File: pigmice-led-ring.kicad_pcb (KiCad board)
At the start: 2 copper layers, 46 x 51 mm, 46 parts, among them J1 Conn_01x02_Female, J2 Conn_01x03_Female, U1 LMR62014XMF

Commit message: Move labels a bit
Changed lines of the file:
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@@
     (tags SOT-23-5)
     (attr smd)
-    (fp_text reference U1 (at 1.972 -2.162839) (layer F.SilkS)
+    (fp_text reference U1 (at 2.099 -2.162839) (layer F.SilkS)
       (effects (font (size 0.75 0.75) (thickness 0.15)))
     )
@@
     (tags resistor)
     (attr smd)
-    (fp_text reference R2 (at 0 1.4 270) (layer F.SilkS)
-      (effects (font (size 0.75 0.75) (thickness 0.15)))
+    (fp_text reference R2 (at 0.044 1.585 270) (layer F.SilkS)
+      (effects (font (size 1 1) (thickness 0.15)))
     )
     (fp_text value 13.3k (at 0 1.65 90) (layer F.Fab)
@@
     (tags capacitor)
     (attr smd)
-    (fp_text reference CF1 (at 1.515 -1.934) (layer F.SilkS)
+    (fp_text reference CF1 (at 1.515 -1.807) (layer F.SilkS)
       (effects (font (size 0.75 0.75) (thickness 0.15)))
     )

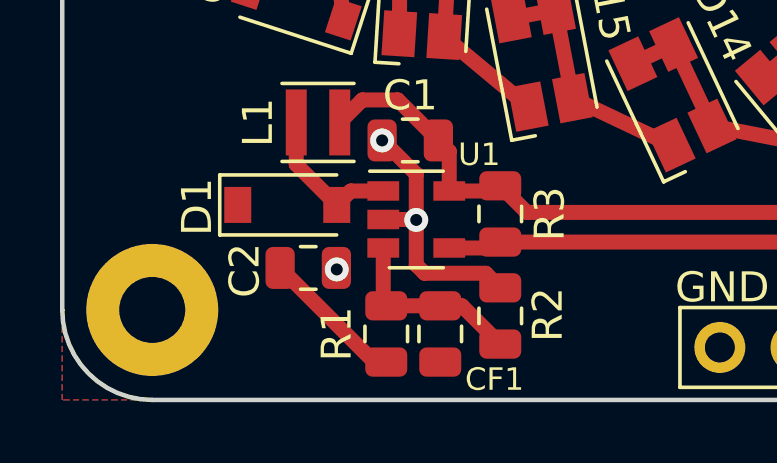
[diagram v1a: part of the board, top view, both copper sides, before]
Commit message: Remove extraneous trace
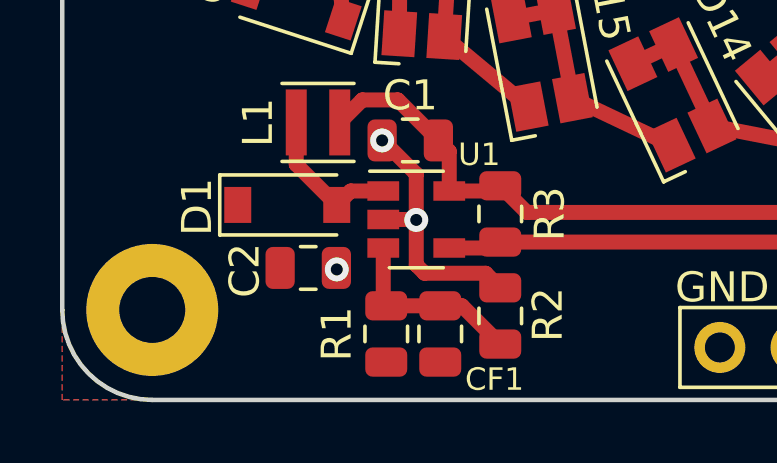
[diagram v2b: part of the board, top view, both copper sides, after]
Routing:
- net /Vled: track 4.84 -> 0.40 mm
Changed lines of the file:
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@@
     (thickness 1.6)
     (drawings 14)
-    (tracks 133)
+    (tracks 132)
     (zones 0)
     (modules 46)
@@
   (via (at 77.6625 99.35) (size 0.8) (drill 0.4) (layers F.Cu B.Cu) (net 1) (status 30))
   (segment (start 77.4 106.7375) (end 77.8 106.7375) (width 0.5) (layer F.Cu) (net 2) (status 30))
-  (segment (start 74.2625 103.6) (end 77.4 106.7375) (width 0.5) (layer F.Cu) (net 2) (status 30))
   (segment (start 77.7 104.7625) (end 77.8 104.8625) (width 0.5) (layer F.Cu) (net 3) (status 30))
   (segment (start 77.7 102.934839) (end 77.7 104.7625) (width 0.5) (layer F.Cu) (net 3) (status 30))

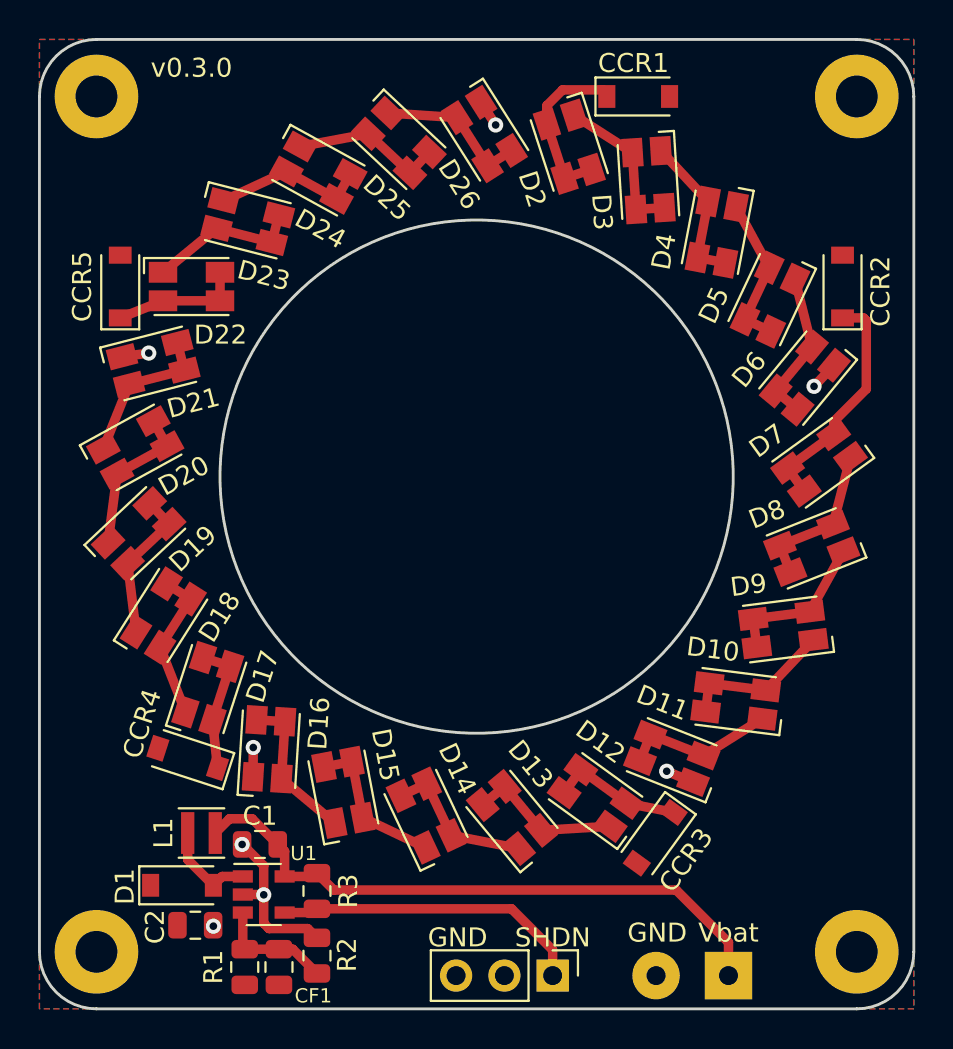
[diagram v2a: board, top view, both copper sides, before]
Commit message: Revision 0.3.1
- Fixes an issue in the LED footprint resulting in a short between the
anode and cathode
- Uses thicker traces where possible
- Moves CCRs for better connections to Vled plane
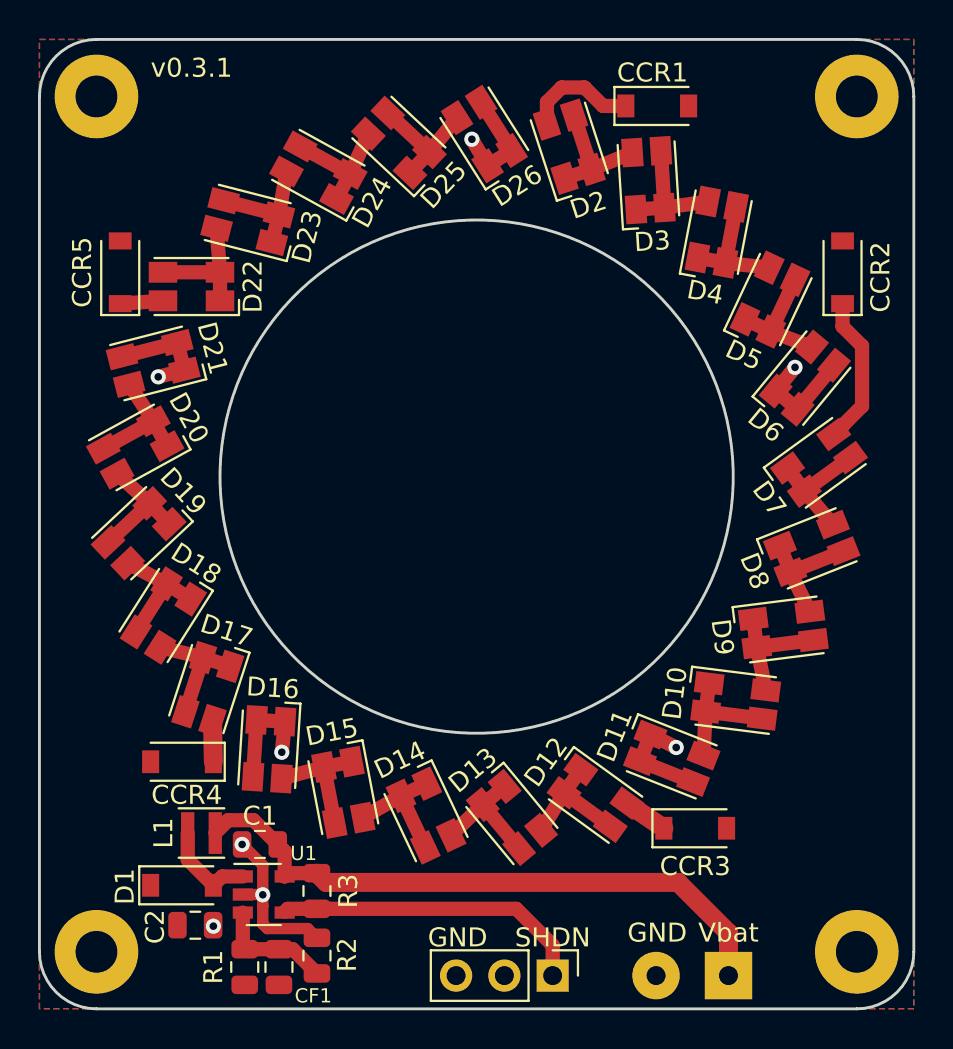
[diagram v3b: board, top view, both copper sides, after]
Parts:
- moved CCR3 2.16 mm to (101.5, 98.5), turned to 0 degrees
- moved CCR1 1.12 mm to (99.5, 60.5)
- moved CCR2 0.75 mm to (109.2, 69.2)
- moved CCR5 0.75 mm to (71.2, 69.2)
- moved CCR4 0.36 mm to (74.5, 95.0), turned to 180 degrees
- turned D10 to 352.8 degrees
- turned D11 to 338.4 degrees
- turned D12 to 324 degrees
- turned D13 to 309.6 degrees
- turned D14 to 295.2 degrees
- turned D15 to 280.8 degrees
- turned D16 to 266.4 degrees
- turned D17 to 252 degrees
- turned D18 to 237.6 degrees
- turned D19 to 223.2 degrees
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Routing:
- net GND: track 16.3 -> 39.1 mm
- net Net-(CCR4-Pad1): track 6.99 -> 2.17 mm
- net Net-(CCR5-Pad1): track 6.92 -> 2.25 mm
- net Net-(CCR3-Pad1): track 7.01 -> 2.34 mm
- net Net-(CCR2-Pad1): track 12.5 -> 7.93 mm
- net Net-(CCR1-Pad1): track 9.20 -> 6.02 mm
- net Net-(D23-Pad1): track 8.15 -> 6.82 mm
- net Net-(D20-Pad1): track 8.15 -> 6.82 mm
- net Net-(D18-Pad1): track 8.15 -> 6.82 mm
- net Net-(D10-Pad2): track 8.15 -> 6.82 mm
- net Net-(D15-Pad1): track 8.15 -> 6.82 mm
- net Net-(D2-Pad1): track 8.15 -> 6.82 mm
- net Net-(D19-Pad1): track 8.15 -> 6.82 mm
- net Net-(D25-Pad1): track 8.15 -> 6.82 mm
- net Net-(D17-Pad1): track 8.15 -> 6.82 mm
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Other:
- board text added: "v0.3.1"
- board text removed: "v0.3.0"

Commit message: Add mini badge
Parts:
- added BT1: Battery_Cell, Battery:BatteryHolder_LINX_BAT-HLD-012-SMT, B.Cu at (90.0, 80.0)
- added D27: LED, LED_SMD:LED_0603_1608Metric, F.Cu at (91.8, 85.5)
- added D28: LED, LED_SMD:LED_0603_1608Metric, F.Cu at (88.2, 87.2)
- added D29: LED, LED_SMD:LED_0603_1608Metric, F.Cu at (91.8, 87.2)
- added D30: LED, LED_SMD:LED_0603_1608Metric, F.Cu at (88.2, 85.5)
- added G***: LOGO, led-ring:logo_silkscreen, F.Cu at (90.0, 77.5)
- added R4: 47Ω, Resistor_SMD:R_0603_1608Metric, F.Cu at (95.0, 85.5)
- added R5: 47Ω, Resistor_SMD:R_0603_1608Metric, F.Cu at (85.0, 87.2)
- added R6: 56Ω, Resistor_SMD:R_0603_1608Metric, F.Cu at (95.0, 87.2)
- added R7: 56Ω, Resistor_SMD:R_0603_1608Metric, F.Cu at (85.0, 85.5)
- added REF**: MountingHole_2.2mm_M2_Pad, MountingHole:MountingHole_2.2mm_M2_Pad, F.Cu at (90.0, 70.5)
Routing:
- net Net-(BT1-Pad1): track 0.00 -> 41.0 mm, vias 0 -> 2
- net Net-(BT1-Pad2): track 0.00 -> 15.9 mm, vias 0 -> 1
- net Net-(D30-Pad2): track 0.00 -> 1.68 mm
- net Net-(D29-Pad2): track 0.00 -> 1.68 mm
- net Net-(D28-Pad2): track 0.00 -> 1.68 mm
- net Net-(D27-Pad2): track 0.00 -> 1.68 mm
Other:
- outline, holes or cut-outs redrawn
- board text added: "v0.3.2"
- board text removed: "v0.3.1"
